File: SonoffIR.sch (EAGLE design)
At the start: 5 parts, among them Q1 2N2222

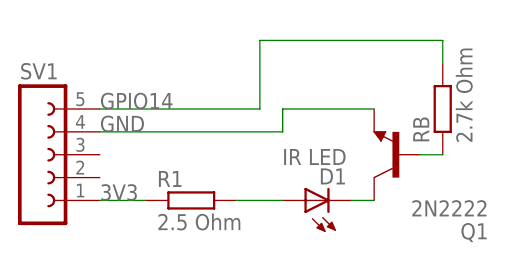
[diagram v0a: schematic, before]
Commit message: Better Name/Value placement on Board
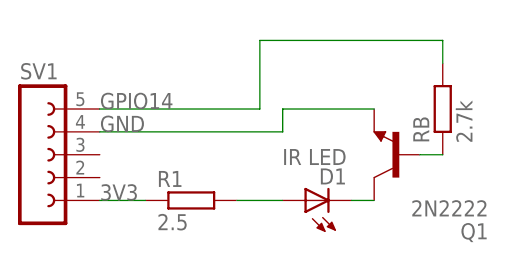
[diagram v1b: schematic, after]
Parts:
- R1: value 2.5 Ohm -> 2.5
- RB: value 2.7k Ohm -> 2.7k
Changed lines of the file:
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@@
 <setting verticaltext="up"/>
 </settings>
-<grid distance="0.1" unitdist="inch" unit="mm" style="lines" multiple="1" display="yes" altdistance="0.01" altunitdist="inch" altunit="mm"/>
+<grid distance="0.1" unitdist="inch" unit="inch" style="lines" multiple="1" display="no" altdistance="0.01" altunitdist="inch" altunit="inch"/>
 <layers>
 <layer number="1" name="Top" color="4" fill="1" visible="no" active="no"/>
@@
 <parts>
 <part name="SV1" library="con-lsta" deviceset="FE05-1" device=""/>
-<part name="R1" library="resistor" deviceset="R-EU_" device="0204/2V" value="2.5 Ohm"/>
-<part name="RB" library="resistor" deviceset="R-EU_" device="0204/2V" value="2.7k Ohm"/>
+<part name="R1" library="resistor" deviceset="R-EU_" device="0204/2V" value="2.5"/>
+<part name="RB" library="resistor" deviceset="R-EU_" device="0204/2V" value="2.7k"/>
 <part name="Q1" library="transistor-npn" deviceset="2N3565" device="" value="2N2222"/>
 <part name="D1" library="led" deviceset="SFH482" device="" value="IR LED"/>

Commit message: Changes in Value placement
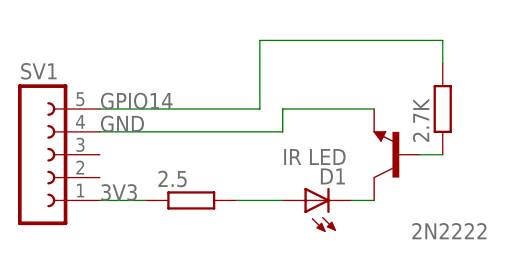
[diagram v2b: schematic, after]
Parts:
- 2.5: value 2.5 -> (none)
- 2.7K: value 2.7k -> (none)
- 2N2222: value 2N2222 -> 2N3565
- renumbered Q1 to 2N2222, R1 to 2.5, RB to 2.7K
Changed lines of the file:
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@@
 <parts>
 <part name="SV1" library="con-lsta" deviceset="FE05-1" device=""/>
-<part name="R1" library="resistor" deviceset="R-EU_" device="0204/2V" value="2.5"/>
-<part name="RB" library="resistor" deviceset="R-EU_" device="0204/2V" value="2.7k"/>
-<part name="Q1" library="transistor-npn" deviceset="2N3565" device="" value="2N2222"/>
+<part name="2.5" library="resistor" deviceset="R-EU_" device="0204/2V"/>
+<part name="2.7K" library="resistor" deviceset="R-EU_" device="0204/2V"/>
+<part name="2N2222" library="transistor-npn" deviceset="2N3565" device="" value=""/>
 <part name="D1" library="led" deviceset="SFH482" device="" value="IR LED"/>
 </parts>
@@
 <instances>
 <instance part="SV1" gate="G$1" x="2.54" y="71.12"/>
-<instance part="R1" gate="G$1" x="20.32" y="66.04"/>
-<instance part="RB" gate="G$1" x="48.26" y="76.2" rot="R90"/>
-<instance part="Q1" gate="G$1" x="43.18" y="71.12" rot="R180"/>
+<instance part="2.5" gate="G$1" x="20.32" y="66.04"/>
+<instance part="2.7K" gate="G$1" x="48.26" y="76.2" rot="R90"/>
+<instance part="2N2222" gate="G$1" x="43.18" y="71.12" rot="R180"/>
 <instance part="D1" gate="1" x="33.02" y="66.04" rot="R90"/>
 </instances>
@@
 <wire x1="27.94" y1="76.2" x2="27.94" y2="83.82" width="0.1524" layer="91"/>
 <wire x1="27.94" y1="83.82" x2="48.26" y2="83.82" width="0.1524" layer="91"/>
-<pinref part="RB" gate="G$1" pin="2"/>
+<pinref part="2.7K" gate="G$1" pin="2"/>
 <wire x1="48.26" y1="83.82" x2="48.26" y2="81.28" width="0.1524" layer="91"/>
 </segment>
@@
 <wire x1="10.16" y1="66.04" x2="15.24" y2="66.04" width="0.1524" layer="91"/>
 <label x="10.16" y="66.04" size="1.778" layer="95"/>
-<pinref part="R1" gate="G$1" pin="1"/>
+<pinref part="2.5" gate="G$1" pin="1"/>
 </segment>
 </net>
@@
 <label x="10.16" y="73.66" size="1.778" layer="95"/>
 <wire x1="30.48" y1="73.66" x2="30.48" y2="76.2" width="0.1524" layer="91"/>
-<pinref part="Q1" gate="G$1" pin="E"/>
+<pinref part="2N2222" gate="G$1" pin="E"/>
 <wire x1="30.48" y1="76.2" x2="40.64" y2="76.2" width="0.1524" layer="91"/>
 </segment>
@@
 <net name="N$1" class="0">
 <segment>
-<pinref part="R1" gate="G$1" pin="2"/>
+<pinref part="2.5" gate="G$1" pin="2"/>
 <pinref part="D1" gate="1" pin="A"/>
 <wire x1="25.4" y1="66.04" x2="30.48" y2="66.04" width="0.1524" layer="91"/>
@@
 <net name="N$2" class="0">
 <segment>
-<pinref part="RB" gate="G$1" pin="1"/>
-<pinref part="Q1" gate="G$1" pin="B"/>
+<pinref part="2.7K" gate="G$1" pin="1"/>
+<pinref part="2N2222" gate="G$1" pin="B"/>
 <wire x1="48.26" y1="71.12" x2="45.72" y2="71.12" width="0.1524" layer="91"/>
 </segment>
@@
 <segment>
 <pinref part="D1" gate="1" pin="C"/>
-<pinref part="Q1" gate="G$1" pin="C"/>
+<pinref part="2N2222" gate="G$1" pin="C"/>
 <wire x1="38.1" y1="66.04" x2="40.64" y2="66.04" width="0.1524" layer="91"/>
 </segment>
